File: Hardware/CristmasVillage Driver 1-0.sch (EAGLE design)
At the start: 5 parts, among them IC1 UA78M05DCY, SW1 POWER

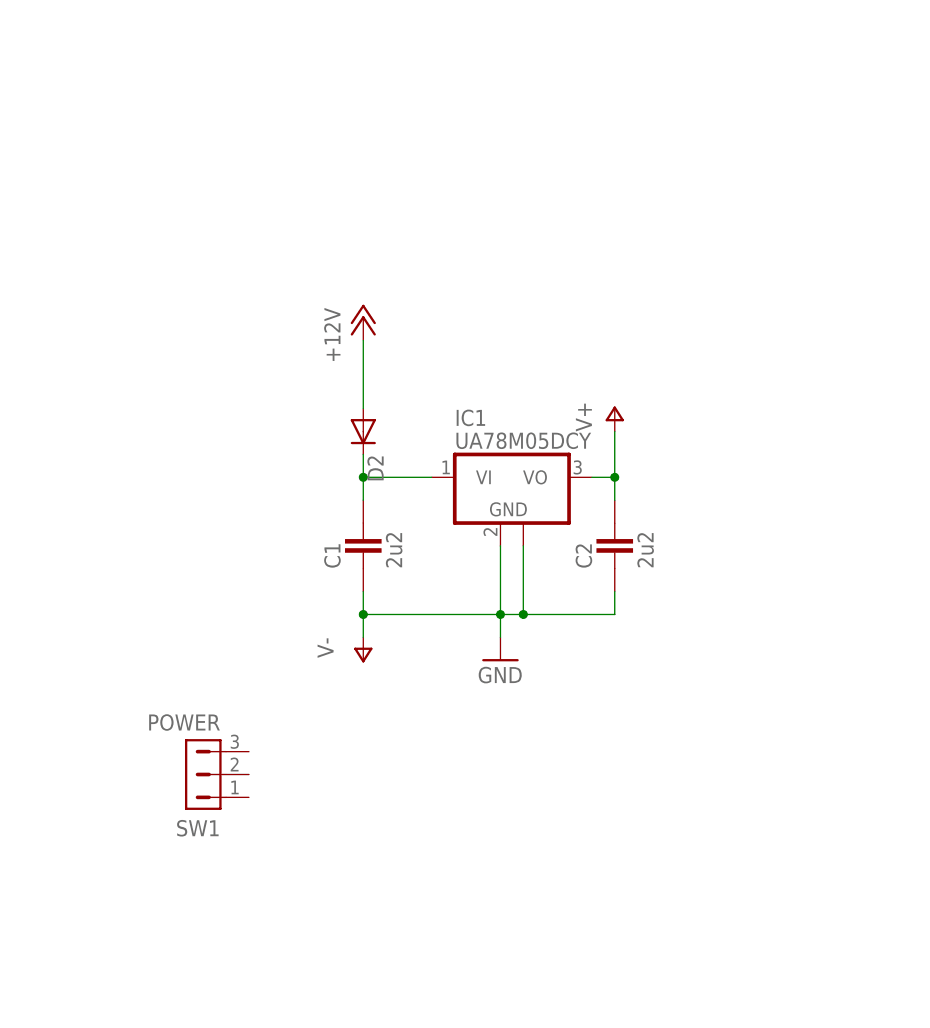
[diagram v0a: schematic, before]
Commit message: Decided on adding light sensor
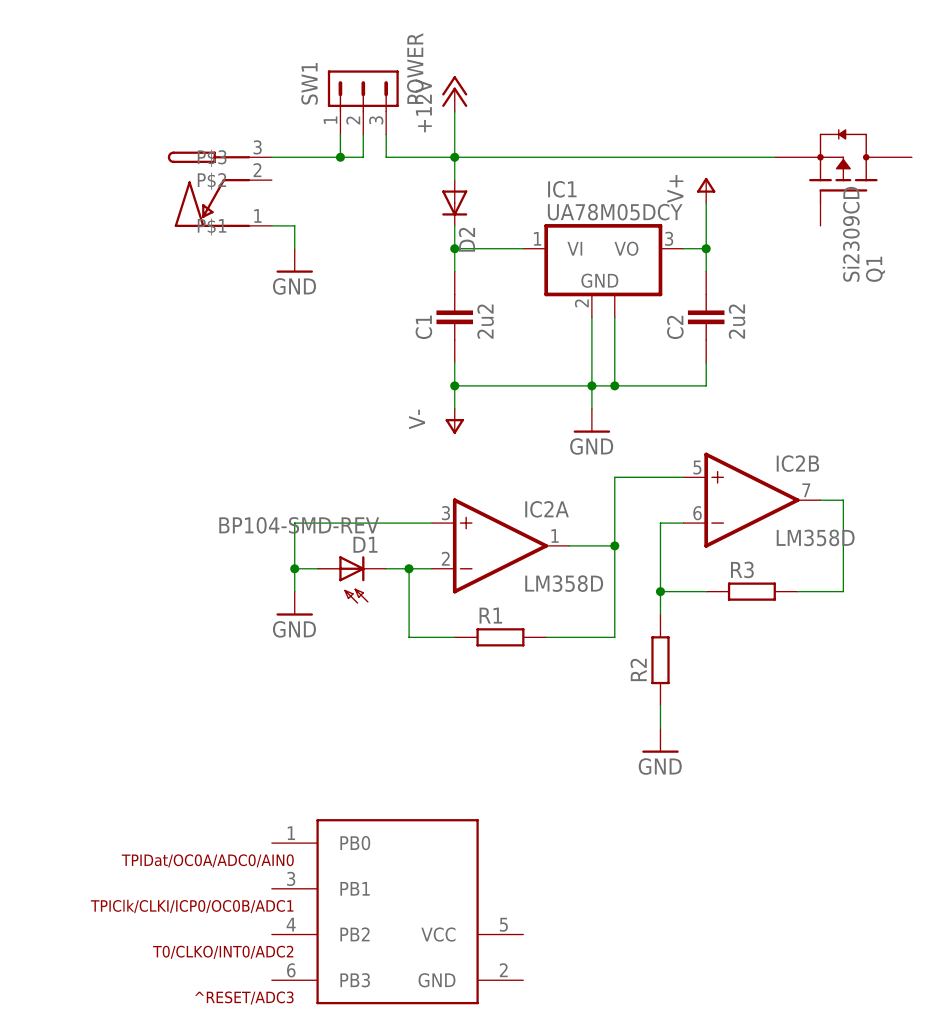
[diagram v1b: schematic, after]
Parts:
- added CN1: MJ-180SMT, con-Multicomp:MJ-180SMT
- added D1: BP104-SMD-REV, Vishay:BP104-SMD-REV
- added IC2: LM358D, linear4:LM358D
- added IC5: ATTINY-4/5/9/10, avr-6:ATTINY-4/5/9/10
- added Q1: Si2309CD, ipc-7351-transistor:MOSFET-PCH_SOT-23
- added R1, R2, R3: (no value), ipc-7351-resistor:RESISTOR_0603
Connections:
- new net N$2: D1.C, IC2A.-IN, R1.1
- new net N$22: CN1.P$3, SW1.1, SW1.2
- new net N$3: IC2A.OUT, IC2B.+IN, R1.2
- new net N$6: IC2B.-IN, R2.2, R3.1
- new net N$7: IC2B.OUT, R3.2
- net +12V: now also Q1.S, SW1.3
- net GND: now also CN1.P$1, D1.A, IC2A.+IN, R2.1
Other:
- moved on the sheet: C1, C2, D2, IC1, SW1

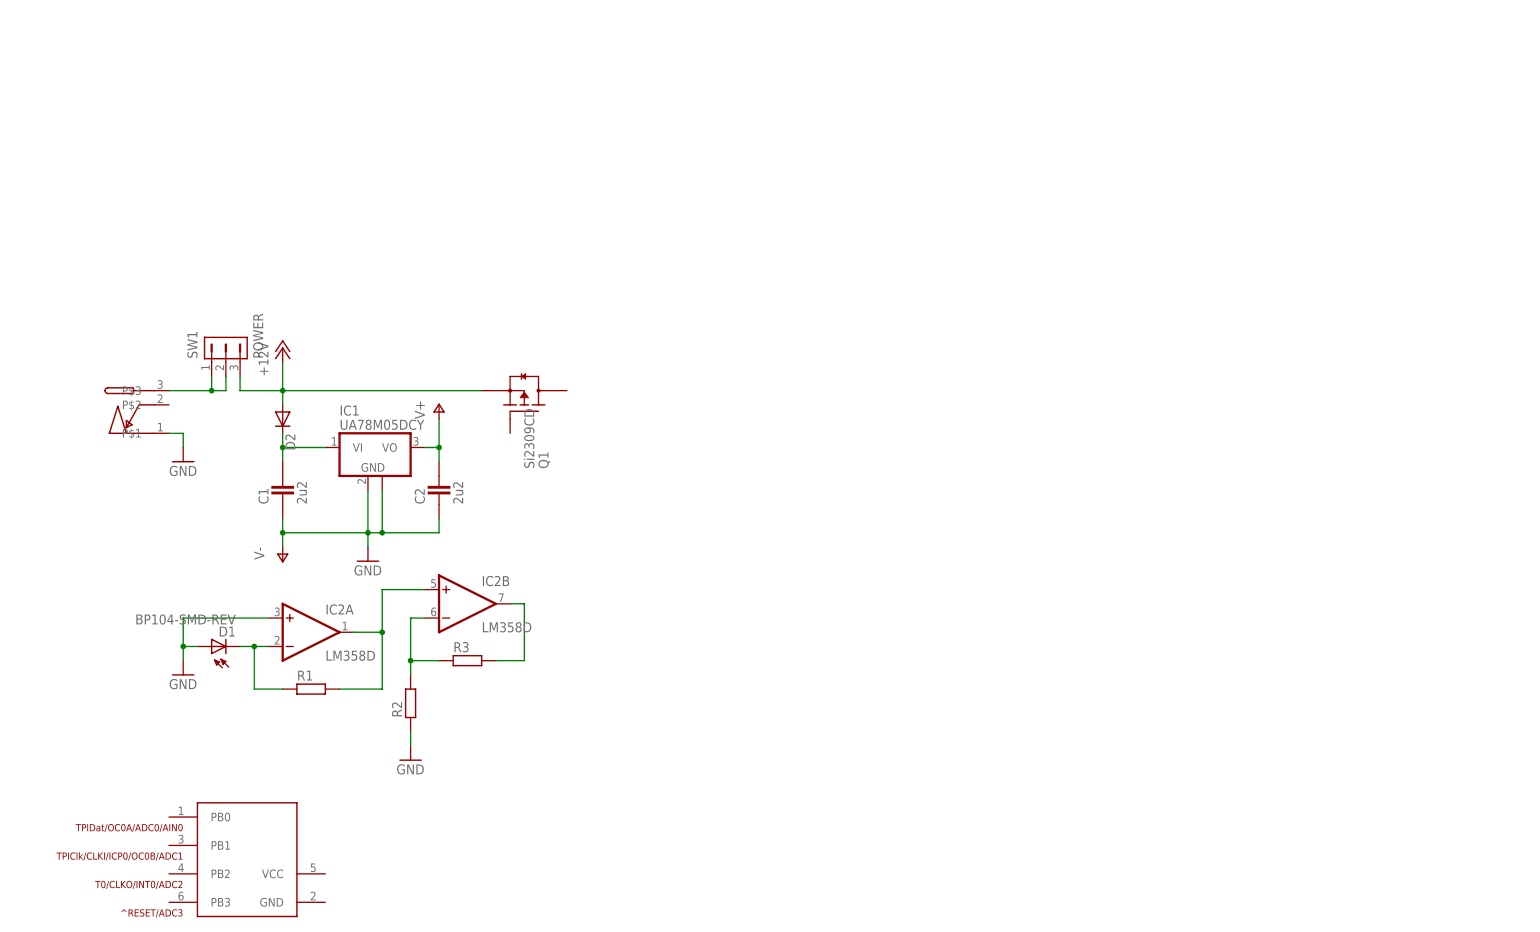
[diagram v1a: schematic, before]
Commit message: Decided on power connector, hooked up dimming, added Tiny2313/4313
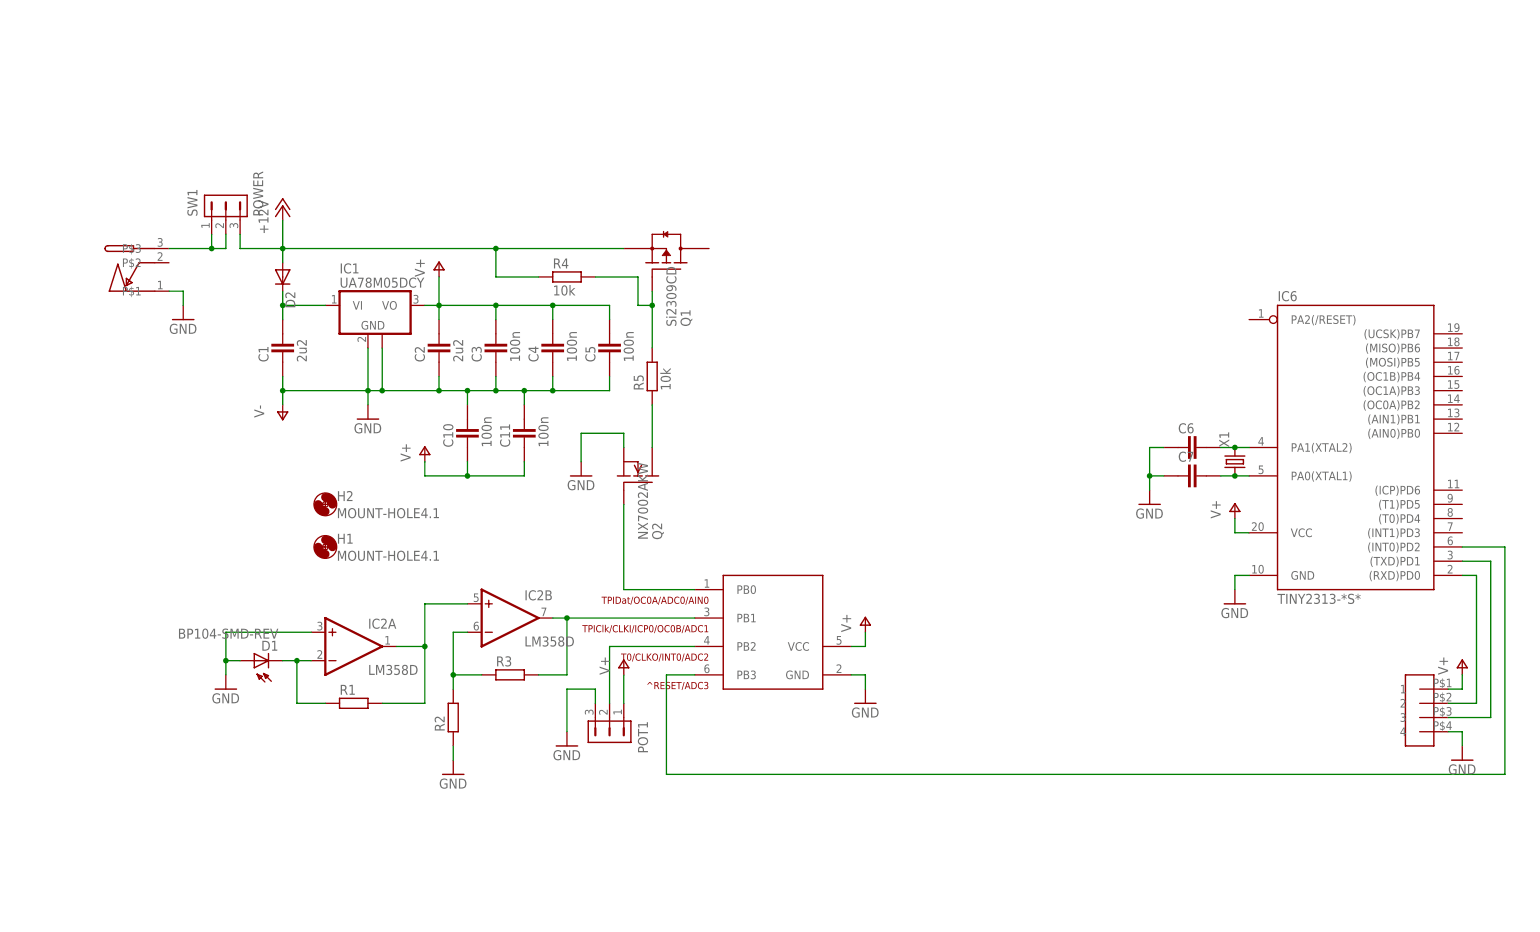
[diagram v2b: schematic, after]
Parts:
- added C10, C11, C3, C4, C5: 100n, ipc-7351-capacitor:CAPACITOR_0603
- added C6, C7: (no value), ipc-7351-capacitor:CAPACITOR_0603
- added CN3-SERIAL: JST-4PSIDE-S4B, Connector-2mm:JST-4PSIDE-S4B
- added H1, H2: MOUNT-HOLE4.1, holes:MOUNT-HOLE4.1
- added IC6: TINY2313-*S*, avr-6:TINY2313-*S*
- added POT1: (no value), con-hdrs40:HDR-1X3-MTE-100
- added Q2: NX7002AKW, ZeroCross Project:NX7002AKW
- added R4, R5: 10k, ipc-7351-resistor:RESISTOR_0603
- added X1: (no value), crystal:CRYSTALSM49
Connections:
- new net N$11: C6.2, IC6.PA1(XTAL2), X1.2
- new net N$12: C7.2, IC6.PA0(XTAL1), X1.1
- new net N$18: IC5.PB3, IC6.(INT0)PD2
- new net N$19: IC5.PB2, POT1.2
- new net N$33: Q1.G, R4.2, R5.2
- new net N$34: Q2.D, R5.1
- new net N$4: CN3-SERIAL.2, IC6.(RXD)PD0
- new net N$5: CN3-SERIAL.3, IC6.(TXD)PD1
- new net N$9: IC5.PB0, Q2.G
- net +12V: now also R4.1
- net GND: now also C10.2, C11.2, C3.1, C4.1, C5.1, C6.1, C7.1, CN3-SERIAL.4, IC5.GND, IC6.GND, POT1.3, Q2.S
- net N$7: now also IC5.PB1
- net V+: now also C10.1, C11.1, C3.2, C4.2, C5.2, CN3-SERIAL.1, IC5.VCC, IC6.VCC, POT1.1
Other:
- moved on the sheet: C1, C2, D1, D2, IC1, IC2A, IC2B, Q1, R1, R2, R3, SW1

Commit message: schematic complete, transferred to board
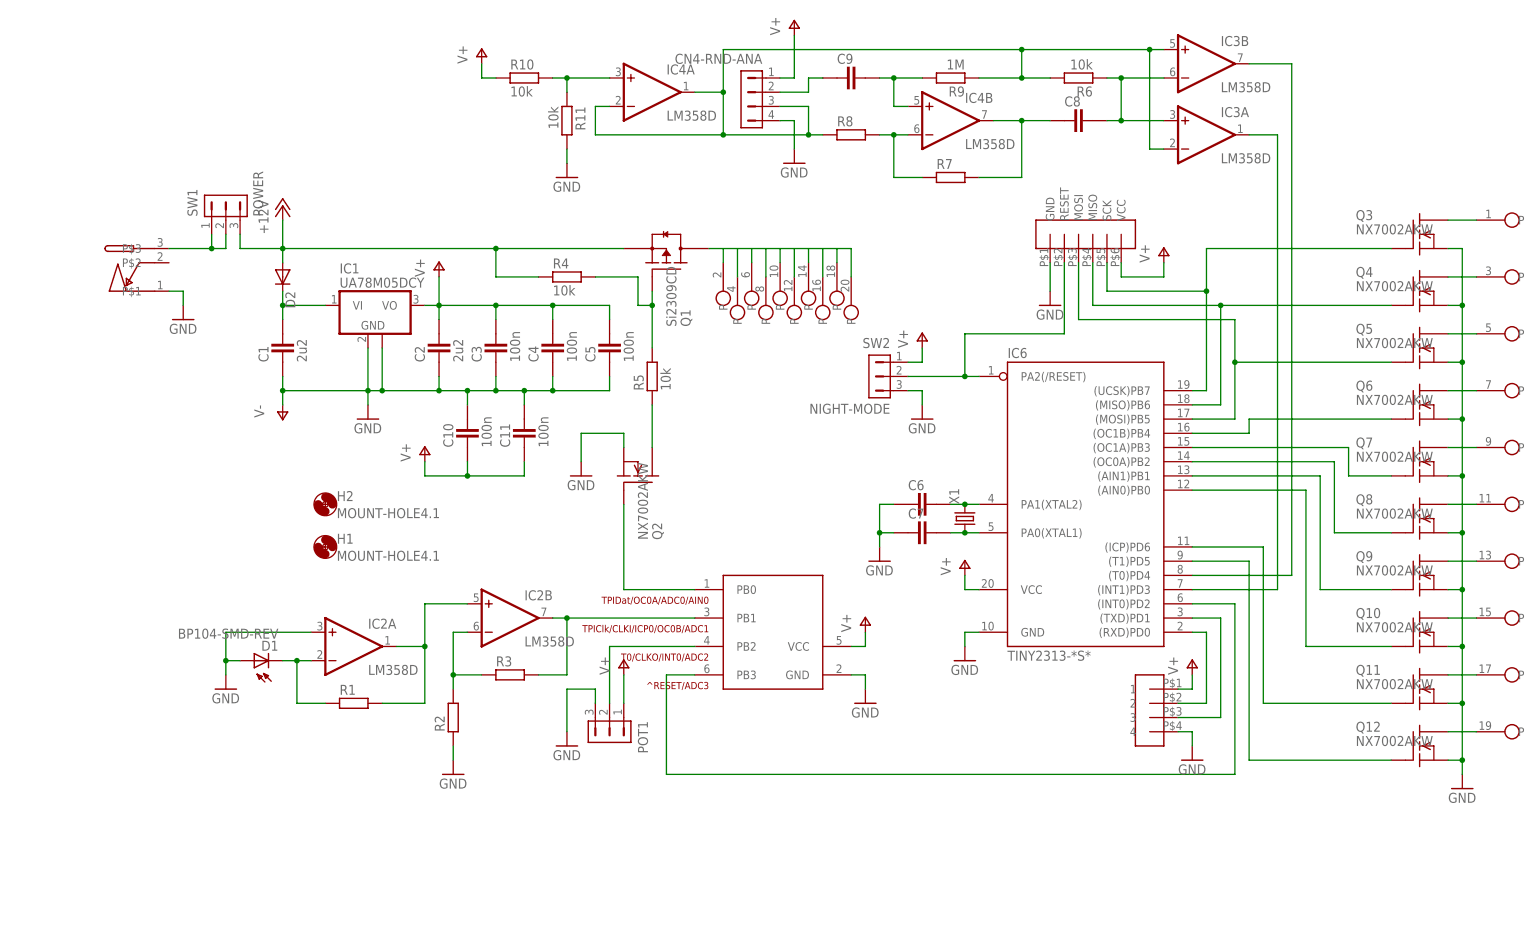
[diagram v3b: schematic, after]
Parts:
- added C8, C9: (no value), ipc-7351-capacitor:CAPACITOR_1206
- added CN2-PROG: JST-6PSPI-SIDE-S6B, avr-6:JST-6PSPI-SIDE-S6B
- added CN4-RND-ANA: (no value), con-hdrs40:HDR-1X4-SIP-100
- added CN5-LEDSTRIPS: HDR_2X10_SIDE-MOUNT, con-SideHeader:HDR_2X10_SIDE-MOUNT
- added IC3, IC4: LM358D, linear4:LM358D
- added Q10, Q11, Q12, Q3, Q4, Q5, Q6, Q7, Q8, Q9: NX7002AKW, ZeroCross Project:NX7002AKW
- added R10, R11, R6: 10k, ipc-7351-resistor:RESISTOR_0603
- added R7, R8: (no value), ipc-7351-resistor:RESISTOR_0603
- added R9: 1M, ipc-7351-resistor:RESISTOR_0603
- added SW2: NIGHT-MODE, con-hdrs40:HDR-1X3-MTE-100
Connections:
- new net HALF-VCC: CN4-RND-ANA.3, IC3A.-IN, IC3B.+IN, IC4A.-IN, IC4A.OUT, R6.2, R8.1, R9.1
- new net MISO: CN2-PROG.MISO, IC6.(MISO)PB6, Q4.G
- new net MOSI: CN2-PROG.MOSI, IC6.(MOSI)PB5, Q5.G
- new net N$10: IC6.(ICP)PD6, Q11.G
- new net N$13: IC6.(AIN0)PB0, Q10.G
- new net N$14: IC6.(AIN1)PB1, Q9.G
- new net N$15: IC6.(OC0A)PB2, Q8.G
- new net N$16: IC6.(OC1A)PB3, Q7.G
- new net N$17: CN2-PROG.RESET, IC6.PA2(/RESET), SW2.2
- new net N$20: IC6.(OC1B)PB4, Q6.G
- new net N$21: CN5-LEDSTRIPSPIN1.P, Q3.D
- new net N$23: CN5-LEDSTRIPSPIN3.P, Q4.D
- new net N$24: CN5-LEDSTRIPSPIN5.P, Q5.D
- new net N$25: CN5-LEDSTRIPSPIN7.P, Q6.D
- new net N$26: CN5-LEDSTRIPSPIN9.P, Q7.D
- new net N$27: CN5-LEDSTRIPSPIN11.P, Q8.D
- new net N$28: CN5-LEDSTRIPSPIN13.P, Q9.D
- new net N$29: CN5-LEDSTRIPSPIN15.P, Q10.D
- new net N$30: CN5-LEDSTRIPSPIN17.P, Q11.D
- new net N$31: CN5-LEDSTRIPSPIN19.P, Q12.D
- new net N$32: CN5-LEDSTRIPSPIN10.P, CN5-LEDSTRIPSPIN12.P, CN5-LEDSTRIPSPIN14.P, CN5-LEDSTRIPSPIN16.P, CN5-LEDSTRIPSPIN18.P, CN5-LEDSTRIPSPIN2.P, CN5-LEDSTRIPSPIN20.P, CN5-LEDSTRIPSPIN4.P, CN5-LEDSTRIPSPIN6.P, CN5-LEDSTRIPSPIN8.P, Q1.D
- new net N$35: IC3A.OUT, IC6.(INT1)PD3
- new net N$36: IC3B.OUT, IC6.(T0)PD4
- new net N$37: C8.2, IC3A.+IN, IC3B.-IN, R6.1
- new net N$38: IC4A.+IN, R10.2, R11.1
- new net N$39: C8.1, IC4B.OUT, R7.2
- new net N$40: IC4B.-IN, R7.1, R8.2
- new net N$41: C9.2, IC4B.+IN, R9.2
- new net N$8: IC6.(T1)PD5, Q12.G
- new net RANDOM-ANALOG-SIG: C9.1, CN4-RND-ANA.2
- new net SCK: CN2-PROG.SCK, IC6.(UCSK)PB7, Q3.G
- net GND: now also CN2-PROG.GND, CN4-RND-ANA.4, Q10.S, Q11.S, Q12.S, Q3.S, Q4.S, Q5.S, Q6.S, Q7.S, Q8.S, Q9.S, R11.2, SW2.3
- net V+: now also CN2-PROG.VCC, CN4-RND-ANA.1, R10.1, SW2.1
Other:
- moved on the sheet: C6, C7, IC6, X1
